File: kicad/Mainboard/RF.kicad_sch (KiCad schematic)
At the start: 125 parts, among them J8 Antenna, Q3 BGA6589, Q7 FDV304P, T1 AFT05MS004NT1, U13 BGA2874, U5 ADF7021, U6 HMC546MS8GETR, U7 LM2904A, X1 12.288MHz

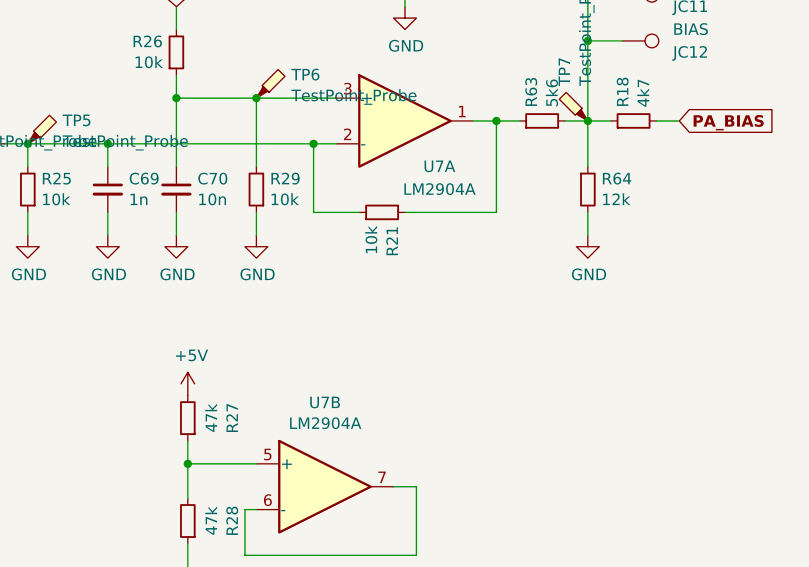
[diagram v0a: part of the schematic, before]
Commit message: Add C106 in parallel to R21
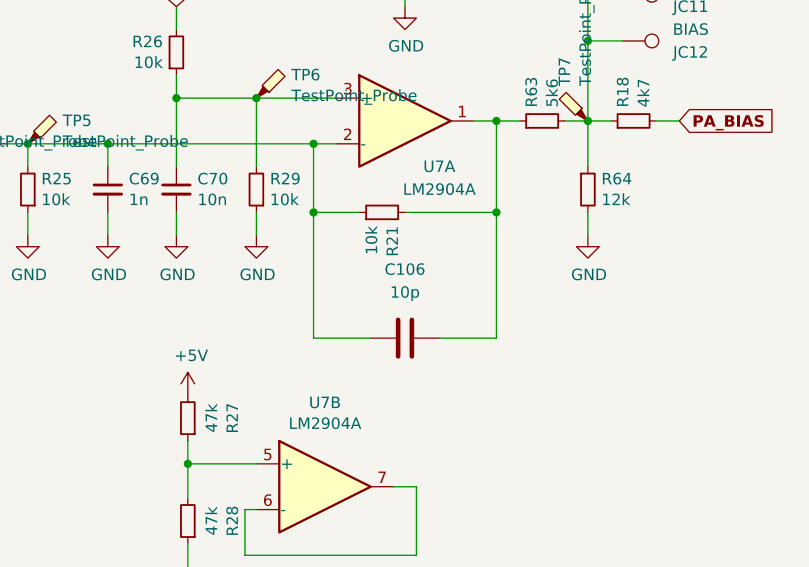
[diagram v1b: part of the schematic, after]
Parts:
- added C106: 10p, symbol Device:C
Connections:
- net at C69.1, R21.1, R24.1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: now also C106.2
- net at R21.2, R63.1, U7.1: now also C106.1
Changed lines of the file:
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@@
   (junction (at 193.04 63.5) (diameter 0) (color 0 0 0 0)
   )
+  (junction (at 359.41 111.76) (diameter 0) (color 0 0 0 0)
+  )
   (junction (at 80.01 160.02) (diameter 0) (color 0 0 0 0)
   )
@@
   (junction (at 234.95 81.28) (diameter 0) (color 0 0 0 0)
   )
+  (junction (at 339.09 111.76) (diameter 0) (color 0 0 0 0)
+  )
   (junction (at 340.36 66.04) (diameter 0) (color 0 0 0 0)
   )
@@
     (stroke (width 0) (type default) (color 0 0 0 0))
   )
+  (wire (pts (xy 339.09 111.76) (xy 339.09 125.73))
+    (stroke (width 0) (type default) (color 0 0 0 0))
+  )
   (wire (pts (xy 140.97 251.46) (xy 140.97 254))
     (stroke (width 0) (type default) (color 0 0 0 0))
@@
     (stroke (width 0) (type default) (color 0 0 0 0))
   )
+  (wire (pts (xy 339.09 125.73) (xy 345.44 125.73))
+    (stroke (width 0) (type default) (color 0 0 0 0))
+  )
   (wire (pts (xy 177.8 138.43) (xy 160.02 138.43))
     (stroke (width 0) (type default) (color 0 0 0 0))
@@
     (stroke (width 0) (type default) (color 0 0 0 0))
   )
-  (wire (pts (xy 344.17 111.76) (xy 339.09 111.76))
-    (stroke (width 0) (type default) (color 0 0 0 0))
-  )
   (wire (pts (xy 207.01 127) (xy 207.01 130.81))
     (stroke (width 0) (type default) (color 0 0 0 0))
@@
     (stroke (width 0) (type default) (color 0 0 0 0))
   )
+  (wire (pts (xy 359.41 125.73) (xy 353.06 125.73))
+    (stroke (width 0) (type default) (color 0 0 0 0))
+  )
   (wire (pts (xy 130.81 194.31) (xy 130.81 181.61))
     (stroke (width 0) (type default) (color 0 0 0 0))
@@
     (stroke (width 0) (type default) (color 0 0 0 0))
   )
+  (wire (pts (xy 359.41 111.76) (xy 359.41 125.73))
+    (stroke (width 0) (type default) (color 0 0 0 0))
+  )
   (wire (pts (xy 161.29 81.28) (xy 161.29 86.36))
     (stroke (width 0) (type default) (color 0 0 0 0))
@@
     (stroke (width 0) (type default) (color 0 0 0 0))
   )
+  (wire (pts (xy 339.09 111.76) (xy 344.17 111.76))
+    (stroke (width 0) (type default) (color 0 0 0 0))
+  )
   (wire (pts (xy 186.69 127) (xy 191.77 127))
     (stroke (width 0) (type default) (color 0 0 0 0))
@@
     (stroke (width 0) (type default) (color 0 0 0 0))
   )
+  (wire (pts (xy 349.25 111.76) (xy 359.41 111.76))
+    (stroke (width 0) (type default) (color 0 0 0 0))
+  )
   (wire (pts (xy 157.48 29.21) (xy 157.48 30.48))
     (stroke (width 0) (type default) (color 0 0 0 0))
@@
     (stroke (width 0) (type default) (color 0 0 0 0))
   )
-  (wire (pts (xy 349.25 111.76) (xy 359.41 111.76))
-    (stroke (width 0) (type default) (color 0 0 0 0))
-  )
   (wire (pts (xy 158.75 217.17) (xy 179.07 217.17))
     (stroke (width 0) (type default) (color 0 0 0 0))
@@
       (effects (font (size 1.27 1.27)) hide)
     )
+    (pin "1")
+    (pin "2")
+  )
+  (symbol (lib_id "Device:C") (at 349.25 125.73 270) (mirror x) (unit 1)
+    (in_bom yes) (on_board yes) (fields_autoplaced)
+    (property "Reference" "C106" (id 0) (at 349.25 118.11 90))
+    (property "Value" "10p" (id 1) (at 349.25 120.65 90))
+    (property "Footprint" "" (id 2) (at 345.44 124.7648 0)
+      (effects (font (size 1.27 1.27)) hide)
+    )
+    (property "Datasheet" "~" (id 3) (at 349.25 125.73 0)
+      (effects (font (size 1.27 1.27)) hide)
+    )
